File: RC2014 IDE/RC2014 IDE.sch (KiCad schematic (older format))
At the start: 10 parts, among them J1 CONN_02X20, J2 Device power, J4 CONN_01X39, U1 74LS138

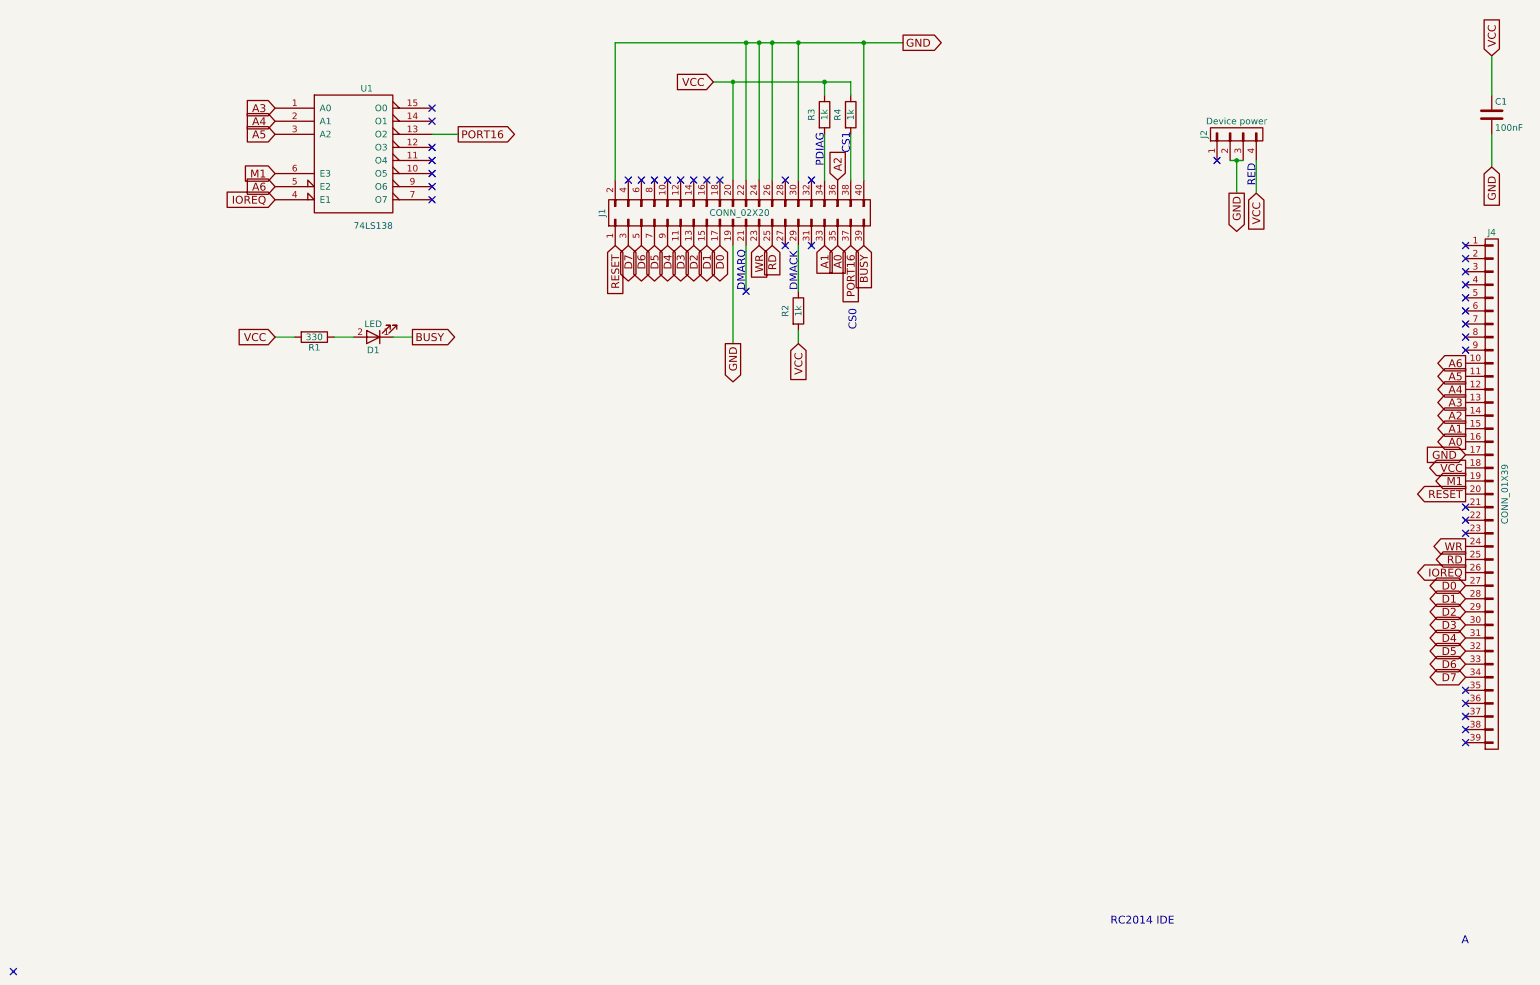
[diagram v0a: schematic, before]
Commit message: Added OR-gates to R/W signals
Seems other people have been having problems when using RD and WR directly, so adding the OR-gates just in case I need them and can't afford to remake the PCBs.
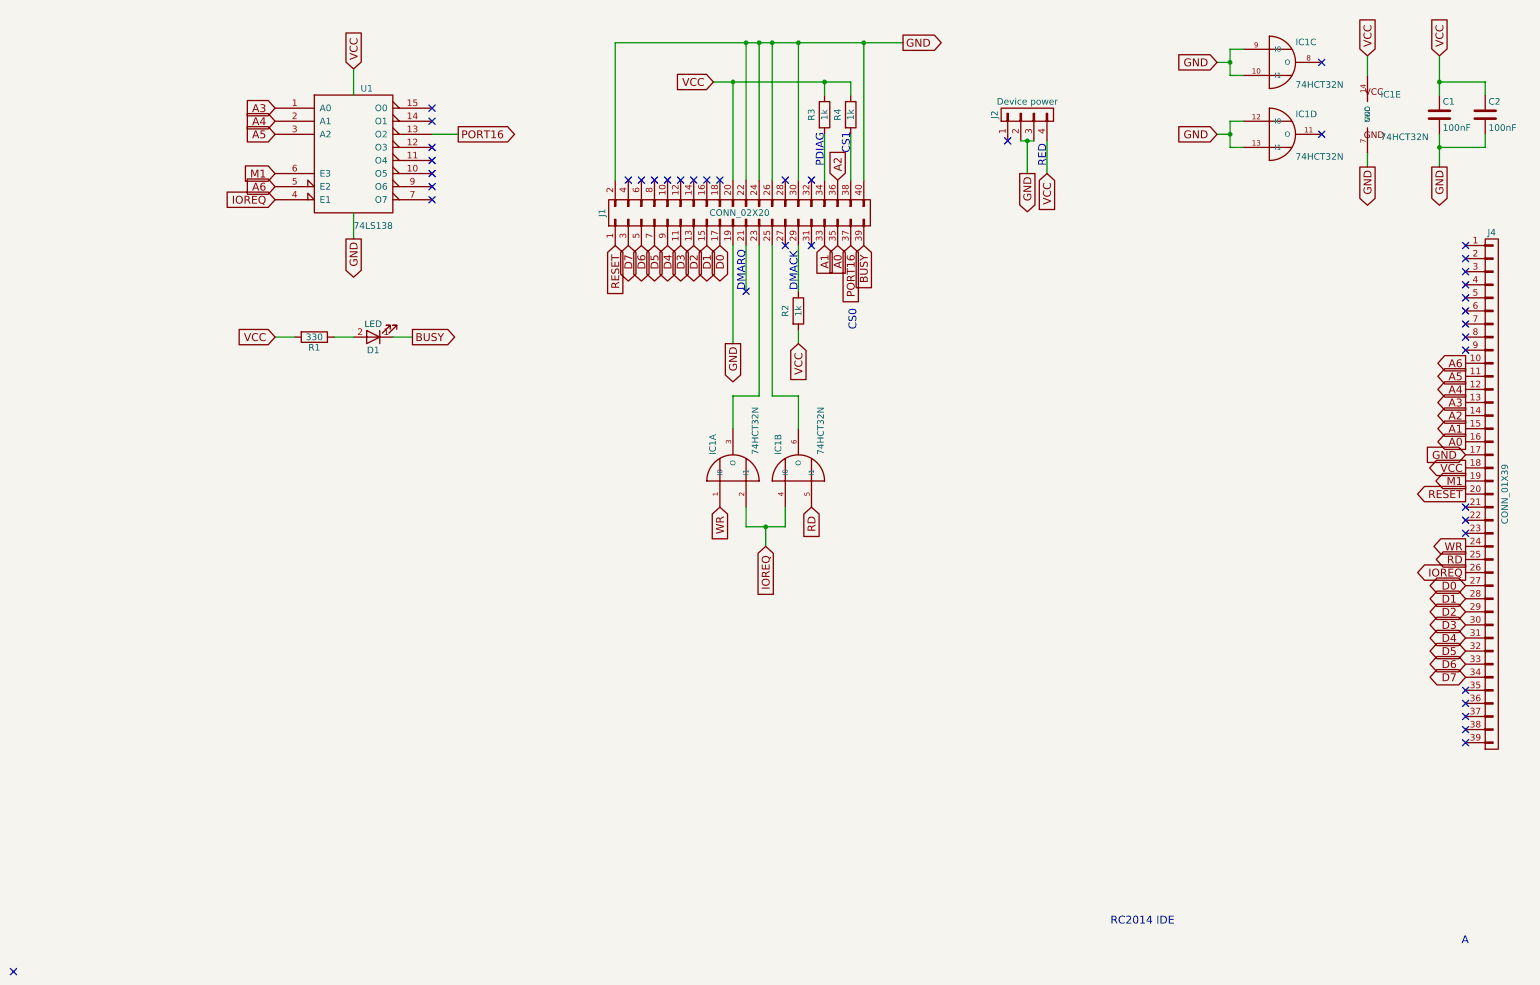
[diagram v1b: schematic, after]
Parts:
- added C2: 100nF, Capacitors_THT:C_Disc_D4.7mm_W2.5mm_P5.00mm, symbol C
- added IC1: 74HCT32N, Housings_DIP:DIP-14_W7.62mm_Socket, symbol 74HCT32N
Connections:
- net GND: now also C2.2, IC1.10 (I1), IC1.12 (I0), IC1.13 (I1), IC1.7 (GND), IC1.9 (I0)
- net IOREQ: now also IC1.2 (I1), IC1.4 (I0)
- net RD: now also IC1.5 (I1); no longer J1.25 (P25)
- net VCC: now also C2.1, IC1.14 (VCC)
- net WR: now also IC1.1 (I0); no longer J1.23 (P23)
- new net: IC1.3 (O), J1.23 (P23)
- new net: IC1.6 (O), J1.25 (P25)
- no-connect marks 39 -> 41
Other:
- moved on the sheet: C1, J2
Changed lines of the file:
@@
 $EndComp
 NoConn ~ 10600 6100
-Text GLabel 10800 850  1    60   Input ~ 0
+Text GLabel 10400 850  1    60   Input ~ 0
 VCC
-Text GLabel 10800 1700 3    60   Input ~ 0
+Text GLabel 10400 1700 3    60   Output ~ 0
 GND
 $Comp
 L C C1
 U 1 1 590DFF2B
-P 10800 1300
-F 0 "C1" H 10825 1400 50  0000 L CNN
-F 1 "100nF" H 10825 1200 50  0000 L CNN
-F 2 "Capacitors_THT:C_Disc_D4.7mm_W2.5mm_P5.00mm" H 10838 1150 50  0001 C CNN
-F 3 "" H 10800 1300 50  0001 C CNN
-	1    10800 1300
+P 10400 1300
+F 0 "C1" H 10425 1400 50  0000 L CNN
+F 1 "100nF" H 10425 1200 50  0000 L CNN
+F 2 "Capacitors_THT:C_Disc_D4.7mm_W2.5mm_P5.00mm" H 10438 1150 50  0001 C CNN
+F 3 "" H 10400 1300 50  0001 C CNN
+	1    10400 1300
 	1    0    0    -1
 $EndComp
@@
 VCC
 Wire Wire Line
-	10800 850  10800 1150
+	10400 850  10400 1150
 Wire Wire Line
-	10800 1450 10800 1700
+	10400 1450 10400 1700
 Wire Wire Line
 	5000 1800 5000 1050
@@
 Text GLabel 4100 2300 3    60   Input ~ 0
 RESET
-Text GLabel 5200 2300 3    60   Input ~ 0
-WR
-Text GLabel 5300 2300 3    60   Input ~ 0
-RD
 Text GLabel 1500 3000 0    60   Input ~ 0
 VCC
@@
 $EndBitmap
 $Bitmap
-Pos 5300 4750
+Pos 5250 6750
 Scale 1.000000
 Data
@@
 L CONN_01X04 J2
 U 1 1 59137E44
-P 8850 1450
-F 0 "J2" H 8850 1700 50  0000 C CNN
-F 1 "Device power" V 8950 1450 50  0000 C CNN
-F 2 "Pin_Headers:Pin_Header_Angled_1x04_Pitch2.54mm" H 8850 1450 50  0001 C CNN
-F 3 "" H 8850 1450 50  0001 C CNN
-	1    8850 1450
+P 7250 1300
+F 0 "J2" H 7250 1550 50  0000 C CNN
+F 1 "Device power" V 7350 1300 50  0000 C CNN
+F 2 "Pin_Headers:Pin_Header_Angled_1x04_Pitch2.54mm" H 7250 1300 50  0001 C CNN
+F 3 "" H 7250 1300 50  0001 C CNN
+	1    7250 1300
 	0    -1   -1   0
 $EndComp
-Text GLabel 8850 1900 3    60   Output ~ 0
+Text GLabel 7250 1750 3    60   Output ~ 0
 GND
 Wire Wire Line
-	8800 1650 8900 1650
+	7200 1500 7300 1500
 Wire Wire Line
-	8850 1650 8850 1900
-Connection ~ 8850 1650
-NoConn ~ 8700 1650
-Text Notes 9000 1850 1    60   ~ 0
+	7250 1500 7250 1750
+Connection ~ 7250 1500
+NoConn ~ 7100 1500
+Text Notes 7400 1700 1    60   ~ 0
 RED
 $Comp
@@
 DMARQ
 NoConn ~ 5100 2650
-Text GLabel 9000 1900 3    60   Input ~ 0
+Text GLabel 7400 1750 3    60   Input ~ 0
 VCC
 Wire Wire Line
-	9000 1650 9000 1900
+	7400 1500 7400 1750
+$Comp
+L 74HCT32N IC1
+U 1 1 5918A6E6
+P 5000 4000
+F 0 "IC1" H 5100 4125 50  0000 L BNN
+F 1 "74HCT32N" H 5100 3800 50  0000 L BNN
+F 2 "Housings_DIP:DIP-14_W7.62mm_Socket" H 5000 4150 50  0001 C CNN
+F 3 "" H 5000 4000 60  0001 C CNN
+	1    5000 4000
+	0    -1   -1   0
+$EndComp
+$Comp
+L 74HCT32N IC1
+U 2 1 5918A723
+P 5500 4000
+F 0 "IC1" H 5600 4125 50  0000 L BNN
+F 1 "74HCT32N" H 5600 3800 50  0000 L BNN
+F 2 "Housings_DIP:DIP-14_W7.62mm_Socket" H 5500 4150 50  0001 C CNN
+F 3 "" H 5500 4000 60  0001 C CNN
+	2    5500 4000
+	0    -1   -1   0
+$EndComp
+$Comp
+L 74HCT32N IC1
+U 3 1 5918A770
+P 9200 900
+F 0 "IC1" H 9300 1025 50  0000 L BNN
+F 1 "74HCT32N" H 9300 700 50  0000 L BNN
+F 2 "Housings_DIP:DIP-14_W7.62mm_Socket" H 9200 1050 50  0001 C CNN
+F 3 "" H 9200 900 60  0001 C CNN
+	3    9200 900
+	1    0    0    -1
+$EndComp
+$Comp
+L 74HCT32N IC1
+U 4 1 5918A7D1
+P 9200 1450
+F 0 "IC1" H 9300 1575 50  0000 L BNN
+F 1 "74HCT32N" H 9300 1250 50  0000 L BNN
+F 2 "Housings_DIP:DIP-14_W7.62mm_Socket" H 9200 1600 50  0001 C CNN
+F 3 "" H 9200 1450 60  0001 C CNN
+	4    9200 1450
+	1    0    0    -1
+$EndComp
+$Comp
+L 74HCT32N IC1
+U 5 1 5918A826
+P 9850 1300
+F 0 "IC1" H 9950 1425 50  0000 L BNN
+F 1 "74HCT32N" H 9950 1100 50  0000 L BNN
+F 2 "Housings_DIP:DIP-14_W7.62mm_Socket" H 9850 1450 50  0001 C CNN
+F 3 "" H 9850 1300 60  0001 C CNN
+	5    9850 1300
+	1    0    0    -1
+$EndComp
+$Comp
+L C C2
+U 1 1 5918B0AB
+P 10750 1300
+F 0 "C2" H 10775 1400 50  0000 L CNN
+F 1 "100nF" H 10775 1200 50  0000 L CNN
+F 2 "Capacitors_THT:C_Disc_D4.7mm_W2.5mm_P5.00mm" H 10788 1150 50  0001 C CNN
+F 3 "" H 10750 1300 50  0001 C CNN
+	1    10750 1300
+	1    0    0    -1
+$EndComp
+Wire Wire Line
+	10750 1150 10750 1050
+Wire Wire Line
+	10750 1050 10400 1050
+Connection ~ 10400 1050
+Wire Wire Line
+	10750 1450 10750 1550
+Wire Wire Line
+	10750 1550 10400 1550
+Connection ~ 10400 1550
+Text GLabel 5250 4600 3    60   Input ~ 0
+IOREQ
+Wire Wire Line
+	5100 4300 5100 4450
+Wire Wire Line
+	5100 4450 5400 4450
+Wire Wire Line
+	5250 4450 5250 4600
+Wire Wire Line
+	5400 4450 5400 4300
+Connection ~ 5250 4450
+Text GLabel 4900 4300 3    60   Input ~ 0
+WR
+Text GLabel 5600 4300 3    60   Input ~ 0
+RD
+Wire Wire Line
+	5200 2300 5200 3450
+Wire Wire Line
+	5300 2300 5300 3450
+Wire Wire Line
+	5500 3700 5500 3450
+Wire Wire Line
+	5500 3450 5300 3450
+Wire Wire Line
+	5000 3700 5000 3450
+Wire Wire Line
+	5000 3450 5200 3450
+Text GLabel 9850 1700 3    60   Output ~ 0
+GND
+Text GLabel 9850 850  1    60   Input ~ 0
+VCC
+Text GLabel 8700 1450 0    60   Input ~ 0
+GND
+Text GLabel 8700 900  0    60   Input ~ 0
+GND
+Wire Wire Line
+	8700 900  8800 900
+Wire Wire Line
+	8800 800  8800 1000
+Wire Wire Line
+	8800 1000 8900 1000
+Wire Wire Line
+	8800 800  8900 800
+Connection ~ 8800 900
+Wire Wire Line
+	8700 1450 8800 1450
+Wire Wire Line
+	8800 1350 8800 1550
+Wire Wire Line
+	8800 1350 8900 1350
+Wire Wire Line
+	8800 1550 8900 1550
+Connection ~ 8800 1450
+Wire Wire Line
+	9850 1700 9850 1600
+Wire Wire Line
+	9850 1000 9850 850
+NoConn ~ 9500 900
+NoConn ~ 9500 1450
+Text GLabel 2100 2250 3    60   Output ~ 0
+GND
+Text GLabel 2100 950  1    60   Input ~ 0
+VCC
+Wire Wire Line
+	2100 950  2100 1150
+Wire Wire Line
+	2100 2050 2100 2250
 $EndSCHEMATC

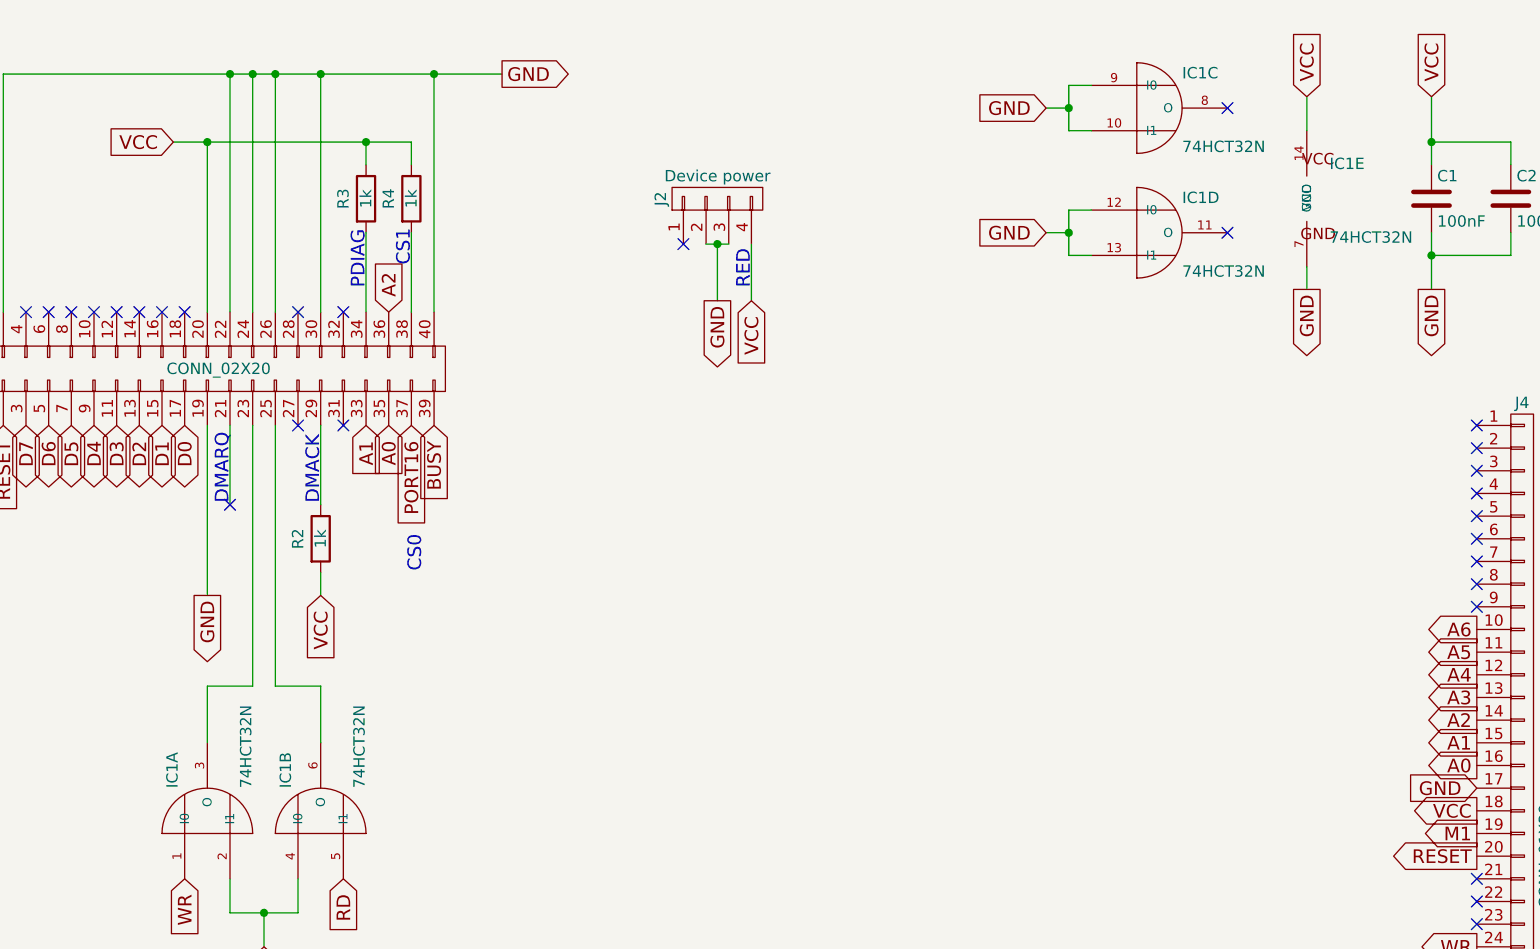
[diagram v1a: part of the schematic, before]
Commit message: Renumbered ICs to be consistent
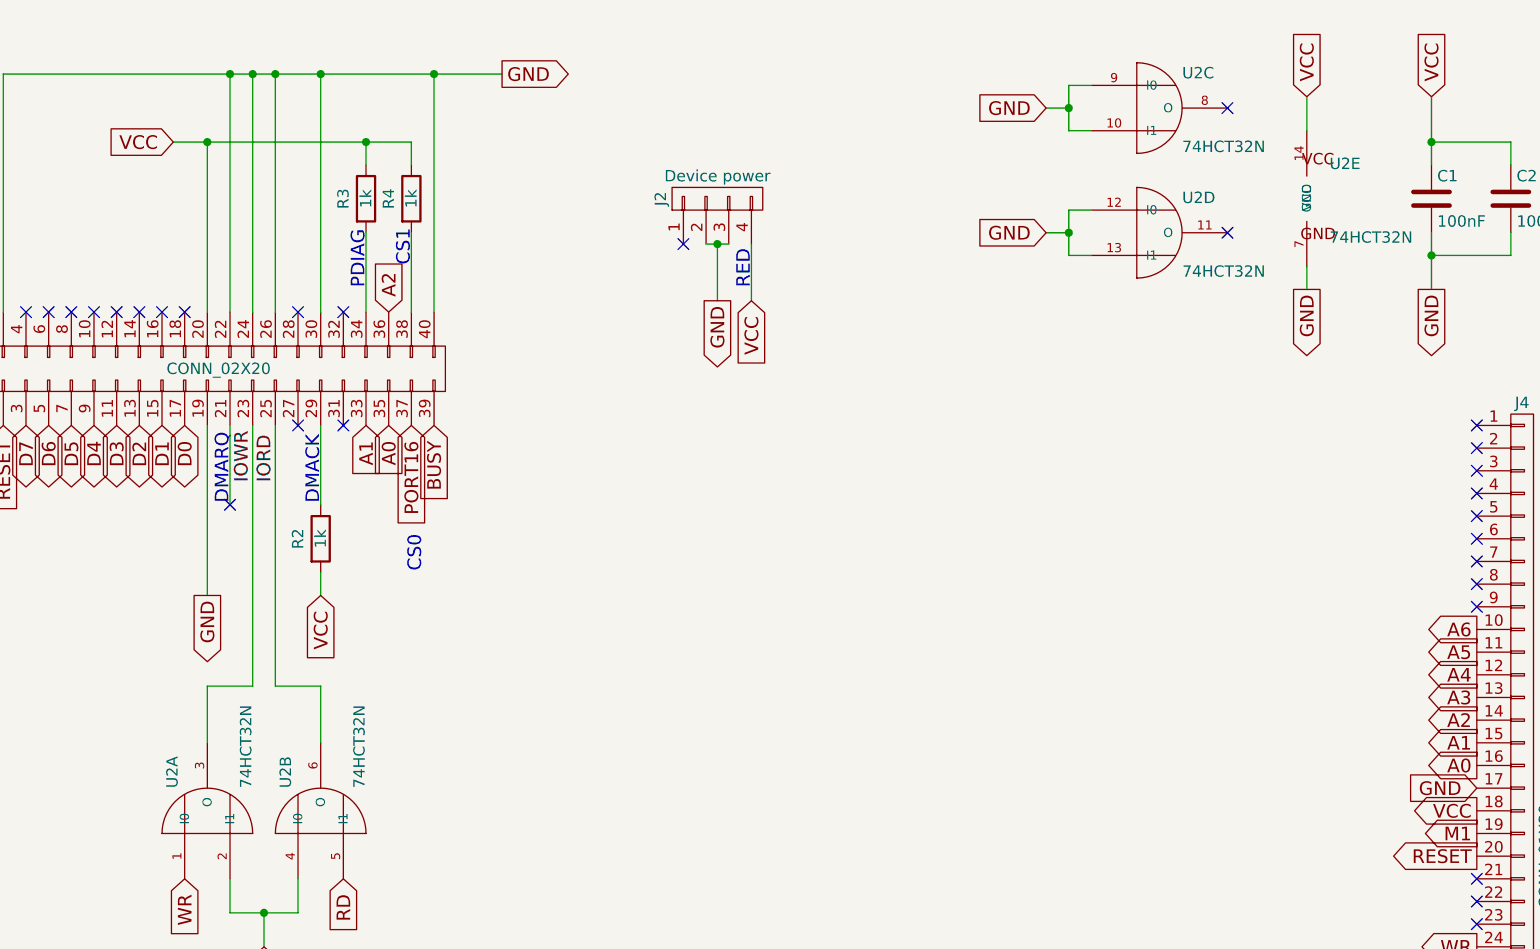
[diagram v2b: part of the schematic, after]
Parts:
- renumbered IC1 to U2
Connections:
- net IOWR: now reaches J1.23 (P23), U2.3 (O)
- net IORD: now reaches J1.25 (P25), U2.6 (O)
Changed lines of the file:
@@
 	7400 1500 7400 1750
 $Comp
-L 74HCT32N IC1
+L 74HCT32N U2
 U 1 1 5918A6E6
 P 5000 4000
-F 0 "IC1" H 5100 4125 50  0000 L BNN
+F 0 "U2" H 5100 4125 50  0000 L BNN
 F 1 "74HCT32N" H 5100 3800 50  0000 L BNN
 F 2 "Housings_DIP:DIP-14_W7.62mm_Socket" H 5000 4150 50  0001 C CNN
@@
 $EndComp
 $Comp
-L 74HCT32N IC1
+L 74HCT32N U2
 U 2 1 5918A723
 P 5500 4000
-F 0 "IC1" H 5600 4125 50  0000 L BNN
+F 0 "U2" H 5600 4125 50  0000 L BNN
 F 1 "74HCT32N" H 5600 3800 50  0000 L BNN
 F 2 "Housings_DIP:DIP-14_W7.62mm_Socket" H 5500 4150 50  0001 C CNN
@@
 $EndComp
 $Comp
-L 74HCT32N IC1
+L 74HCT32N U2
 U 3 1 5918A770
 P 9200 900
-F 0 "IC1" H 9300 1025 50  0000 L BNN
+F 0 "U2" H 9300 1025 50  0000 L BNN
 F 1 "74HCT32N" H 9300 700 50  0000 L BNN
 F 2 "Housings_DIP:DIP-14_W7.62mm_Socket" H 9200 1050 50  0001 C CNN
@@
 $EndComp
 $Comp
-L 74HCT32N IC1
+L 74HCT32N U2
 U 4 1 5918A7D1
 P 9200 1450
-F 0 "IC1" H 9300 1575 50  0000 L BNN
+F 0 "U2" H 9300 1575 50  0000 L BNN
 F 1 "74HCT32N" H 9300 1250 50  0000 L BNN
 F 2 "Housings_DIP:DIP-14_W7.62mm_Socket" H 9200 1600 50  0001 C CNN
@@
 $EndComp
 $Comp
-L 74HCT32N IC1
+L 74HCT32N U2
 U 5 1 5918A826
 P 9850 1300
-F 0 "IC1" H 9950 1425 50  0000 L BNN
+F 0 "U2" H 9950 1425 50  0000 L BNN
 F 1 "74HCT32N" H 9950 1100 50  0000 L BNN
 F 2 "Housings_DIP:DIP-14_W7.62mm_Socket" H 9850 1450 50  0001 C CNN
@@
 Wire Wire Line
 	2100 2050 2100 2250
+Text Label 5300 2550 1    60   ~ 0
+IORD
+Text Label 5200 2550 1    60   ~ 0
+IOWR
 $EndSCHEMATC
